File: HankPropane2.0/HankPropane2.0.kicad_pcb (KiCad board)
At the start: 2 copper layers, 31.3 x 46.3 mm, 9 parts, among them X1 sao_v169bis

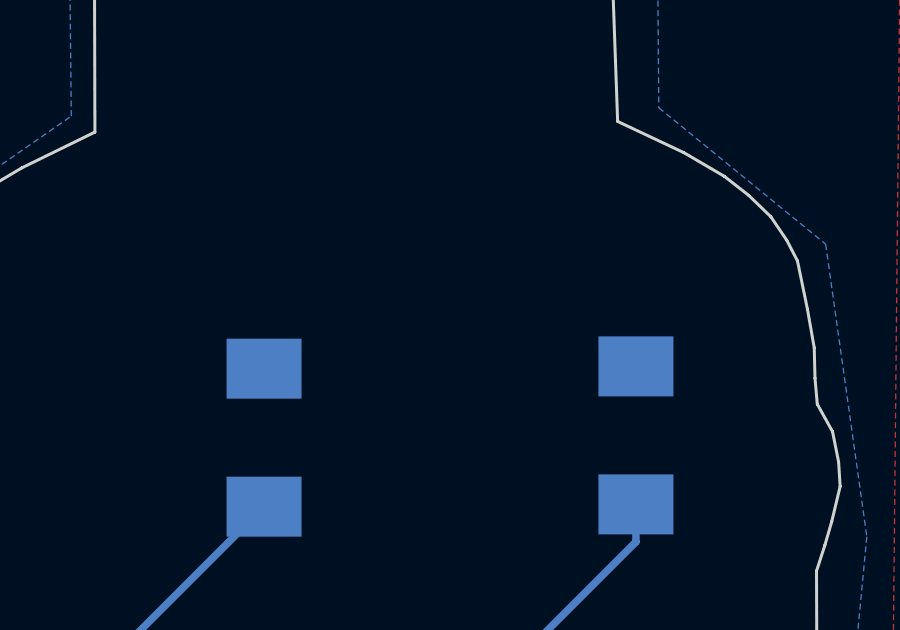
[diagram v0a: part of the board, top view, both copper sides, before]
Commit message: Added 68.1 ohm current limiting resistors and turbo mode jumpers
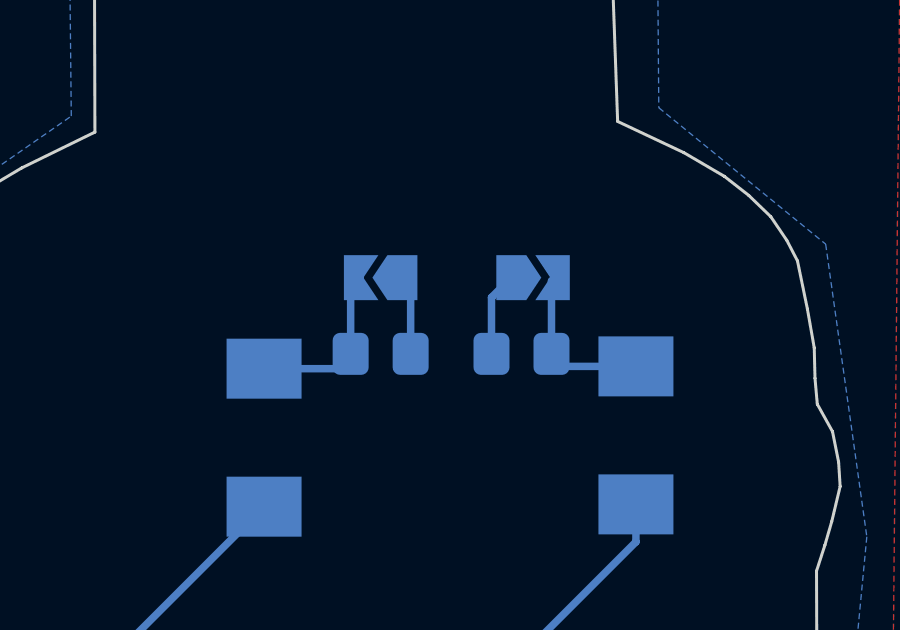
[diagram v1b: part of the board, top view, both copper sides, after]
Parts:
- added JP1: JUMPER-SMT_2_NO, Jumper:SolderJumper-2_P1.3mm_Open_TrianglePad1.0x1.5mm, B.Cu at (185.4, 91.4)
- added JP2: JUMPER-SMT_2_NO, Jumper:SolderJumper-2_P1.3mm_Open_TrianglePad1.0x1.5mm, B.Cu at (180.3, 91.4)
- added R1: 68.1, Resistor_SMD:R_0805_2012Metric_Pad1.20x1.40mm_HandSolder, B.Cu at (185.0, 94.0)
- added R2: 68.1, Resistor_SMD:R_0805_2012Metric_Pad1.20x1.40mm_HandSolder, B.Cu at (180.3, 94.0)
- X1: value sao_v169bis -> Badgelife_sao_connector_v169bis
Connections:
- D1 pad 1: GND -> Net-(D1-K)
- D2 pad 1: GND -> Net-(D2-K)
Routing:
- net Net-(D2-K): track 0.00 -> 5.74 mm
- net Net-(D1-K): track 0.00 -> 5.57 mm
- net GND: track 0.00 -> 5.47 mm

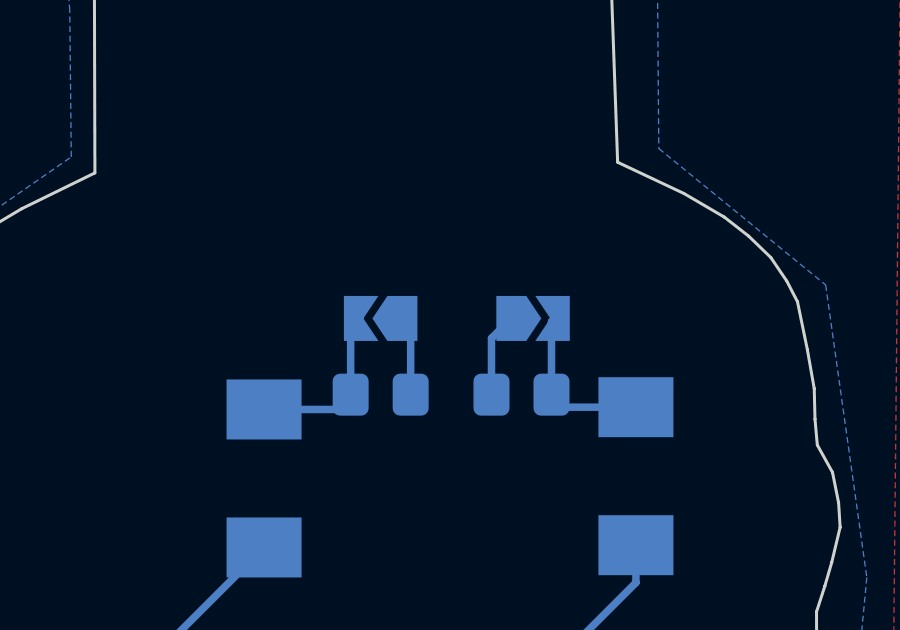
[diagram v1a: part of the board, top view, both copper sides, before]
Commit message: Changed resistors to 1206
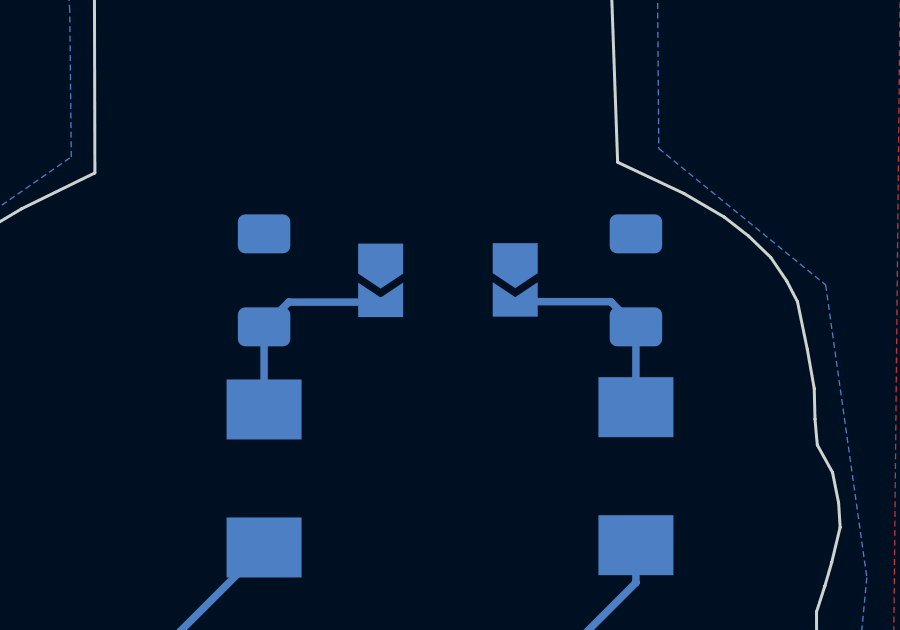
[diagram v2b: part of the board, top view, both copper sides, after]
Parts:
- R1, R2: footprint Resistor_SMD:R_0805_2012Metric_Pad1.20x1.40mm_HandSolder -> Resistor_SMD:R_1206_3216Metric_Pad1.30x1.75mm_HandSolder
- moved R2 5.44 mm to (176.5, 90.2), turned to -90 degrees
- moved R1 5.39 mm to (188.8, 90.2), turned to -90 degrees
- moved JP1 1.42 mm to (184.8, 90.2), turned to -90 degrees
- moved JP2 1.27 mm to (180.3, 90.2), turned to -90 degrees
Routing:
- net GND: track 5.47 -> 0.00 mm
- net Net-(D1-K): track 5.57 -> 7.05 mm
- net Net-(D2-K): track 5.74 -> 6.98 mm
